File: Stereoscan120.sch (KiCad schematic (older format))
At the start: 2 parts

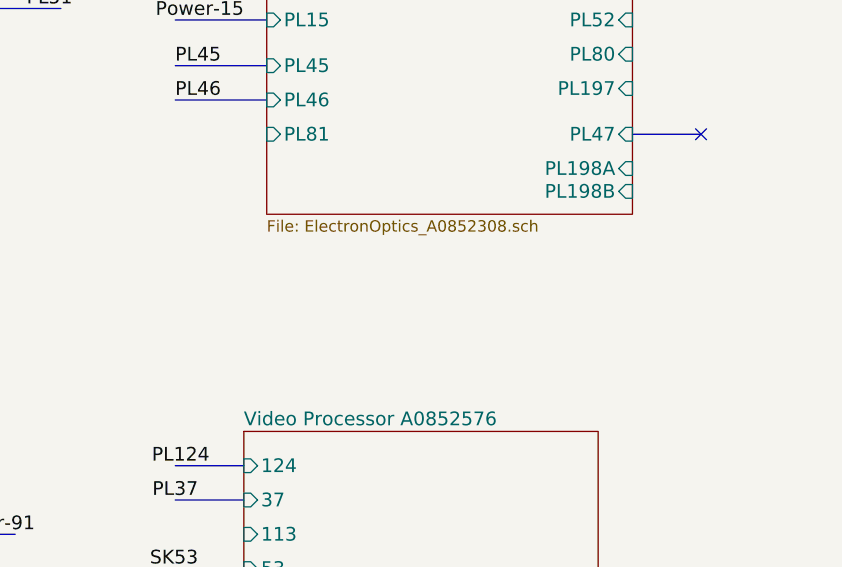
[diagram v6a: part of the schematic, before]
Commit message: Adds EOProm Board PCB
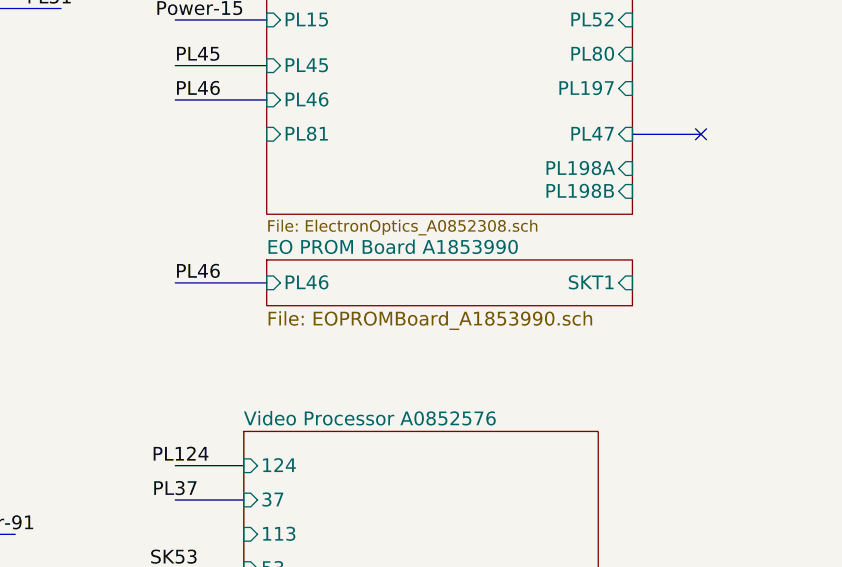
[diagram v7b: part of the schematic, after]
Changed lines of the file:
@@
 $Descr A3 16535 11693
 encoding utf-8
-Sheet 1 17
+Sheet 1 18
 Title ""
 Date ""
@@
 	10000 4200 10300 4200
 NoConn ~ 10300 4200
+$Sheet
+S 8400 4750 1600 200
+U 5B100F42
+F0 "EO PROM Board A1853990" 60
+F1 "EOPROMBoard_A1853990.sch" 60
+F2 "SKT1" I R 10000 4850 60
+F3 "PL46" I L 8400 4850 60
+$EndSheet
+Wire Bus Line
+	8400 4850 8000 4850
+Text Label 8200 4850 2    60   ~ 0
+PL46
 $EndSCHEMATC

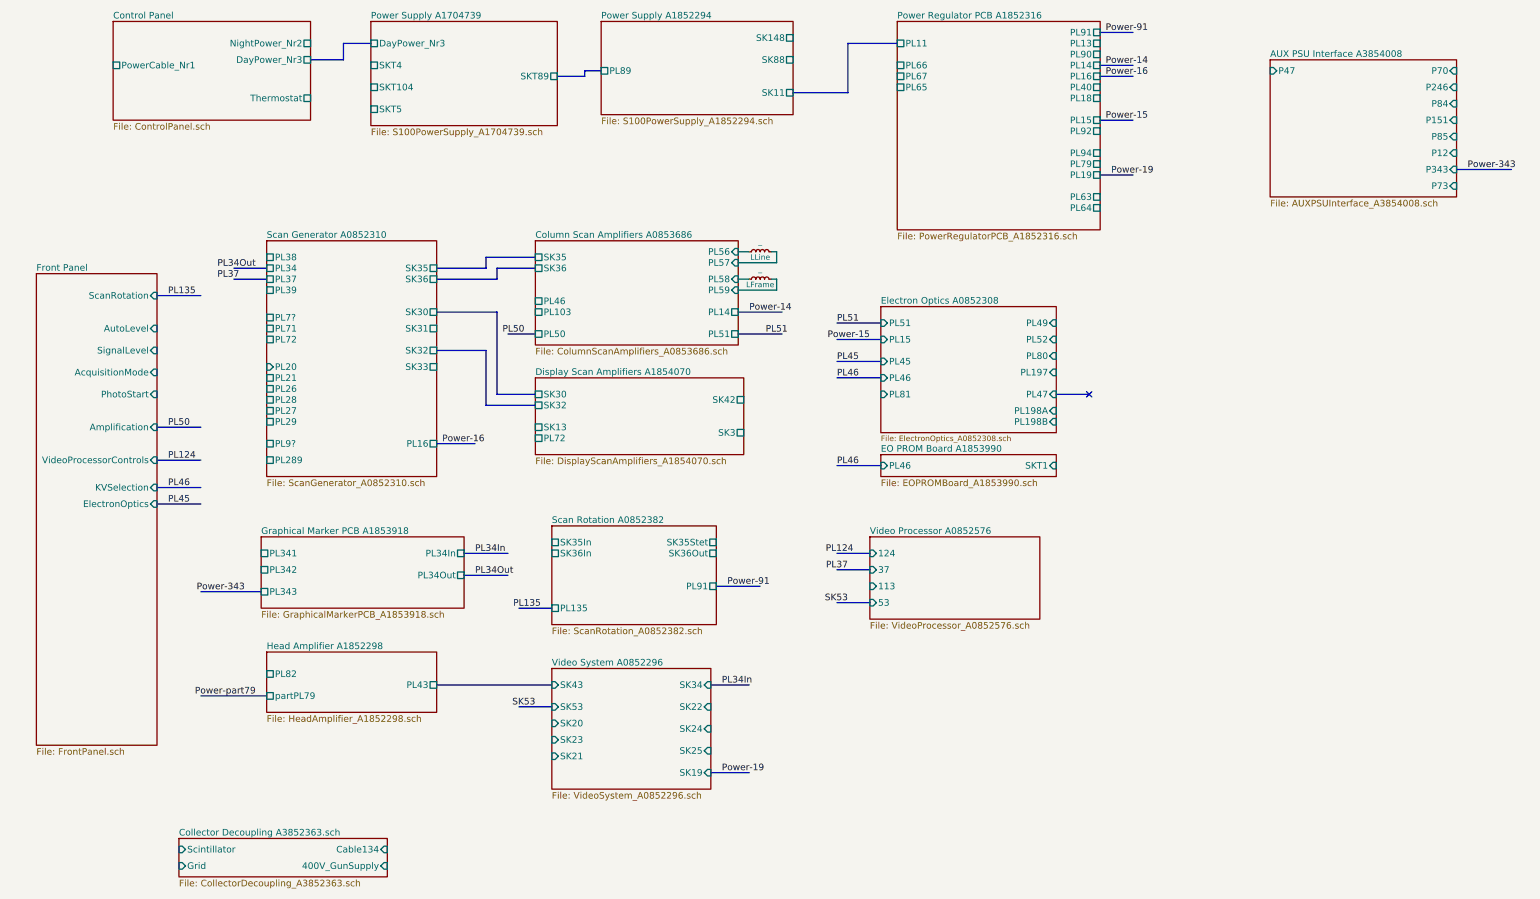
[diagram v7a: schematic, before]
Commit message: Adds Beam Modulation PCB
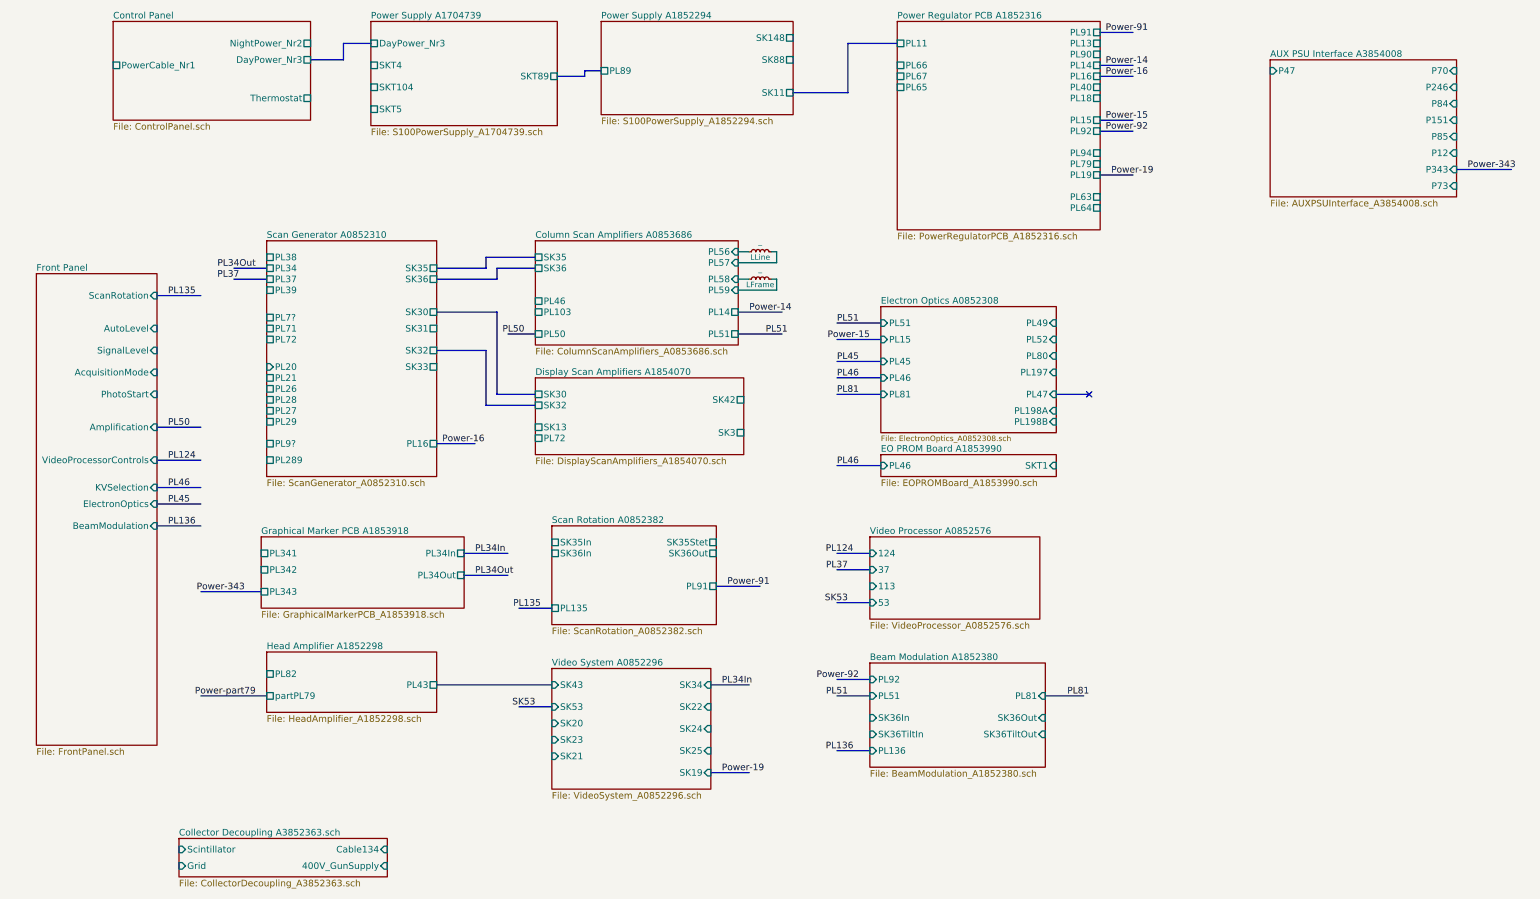
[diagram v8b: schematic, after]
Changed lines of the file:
@@
 $Descr A3 16535 11693
 encoding utf-8
-Sheet 1 18
+Sheet 1 19
 Title ""
 Date ""
@@
 F9 "KVSelection" I R 1800 5050 60
 F10 "ElectronOptics" I R 1800 5200 60
+F11 "BeamModulation" I R 1800 5400 60
 $EndSheet
 Text Label 1900 4500 0    60   ~ 0
@@
 Text Label 8200 4850 2    60   ~ 0
 PL46
+$Sheet
+S 8300 6650 1600 950
+U 5B10EE60
+F0 "Beam Modulation A1852380" 60
+F1 "BeamModulation_A1852380.sch" 60
+F2 "PL51" I L 8300 6950 60
+F3 "PL92" I L 8300 6800 60
+F4 "SK36In" I L 8300 7150 60
+F5 "SK36TiltIn" I L 8300 7300 60
+F6 "SK36Out" I R 9900 7150 60
+F7 "SK36TiltOut" I R 9900 7300 60
+F8 "PL81" I R 9900 6950 60
+F9 "PL136" I L 8300 7450 60
+$EndSheet
+Wire Bus Line
+	10400 1800 10700 1800
+Text Label 10450 1800 0    60   ~ 0
+Power-92
+Wire Bus Line
+	8300 6800 8000 6800
+Text Label 8200 6800 2    60   ~ 0
+Power-92
+Wire Bus Line
+	8300 6950 8000 6950
+Text Label 8100 6950 2    60   ~ 0
+PL51
+Wire Bus Line
+	1800 5400 2200 5400
+Text Label 1900 5400 0    60   ~ 0
+PL136
+Wire Bus Line
+	8300 7450 8000 7450
+Text Label 8150 7450 2    60   ~ 0
+PL136
+Wire Bus Line
+	8400 4200 8000 4200
+Text Label 8200 4200 2    60   ~ 0
+PL81
+Wire Bus Line
+	9900 6950 10250 6950
+Text Label 10100 6950 0    60   ~ 0
+PL81
 $EndSCHEMATC
